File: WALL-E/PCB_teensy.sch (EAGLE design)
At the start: 44 parts

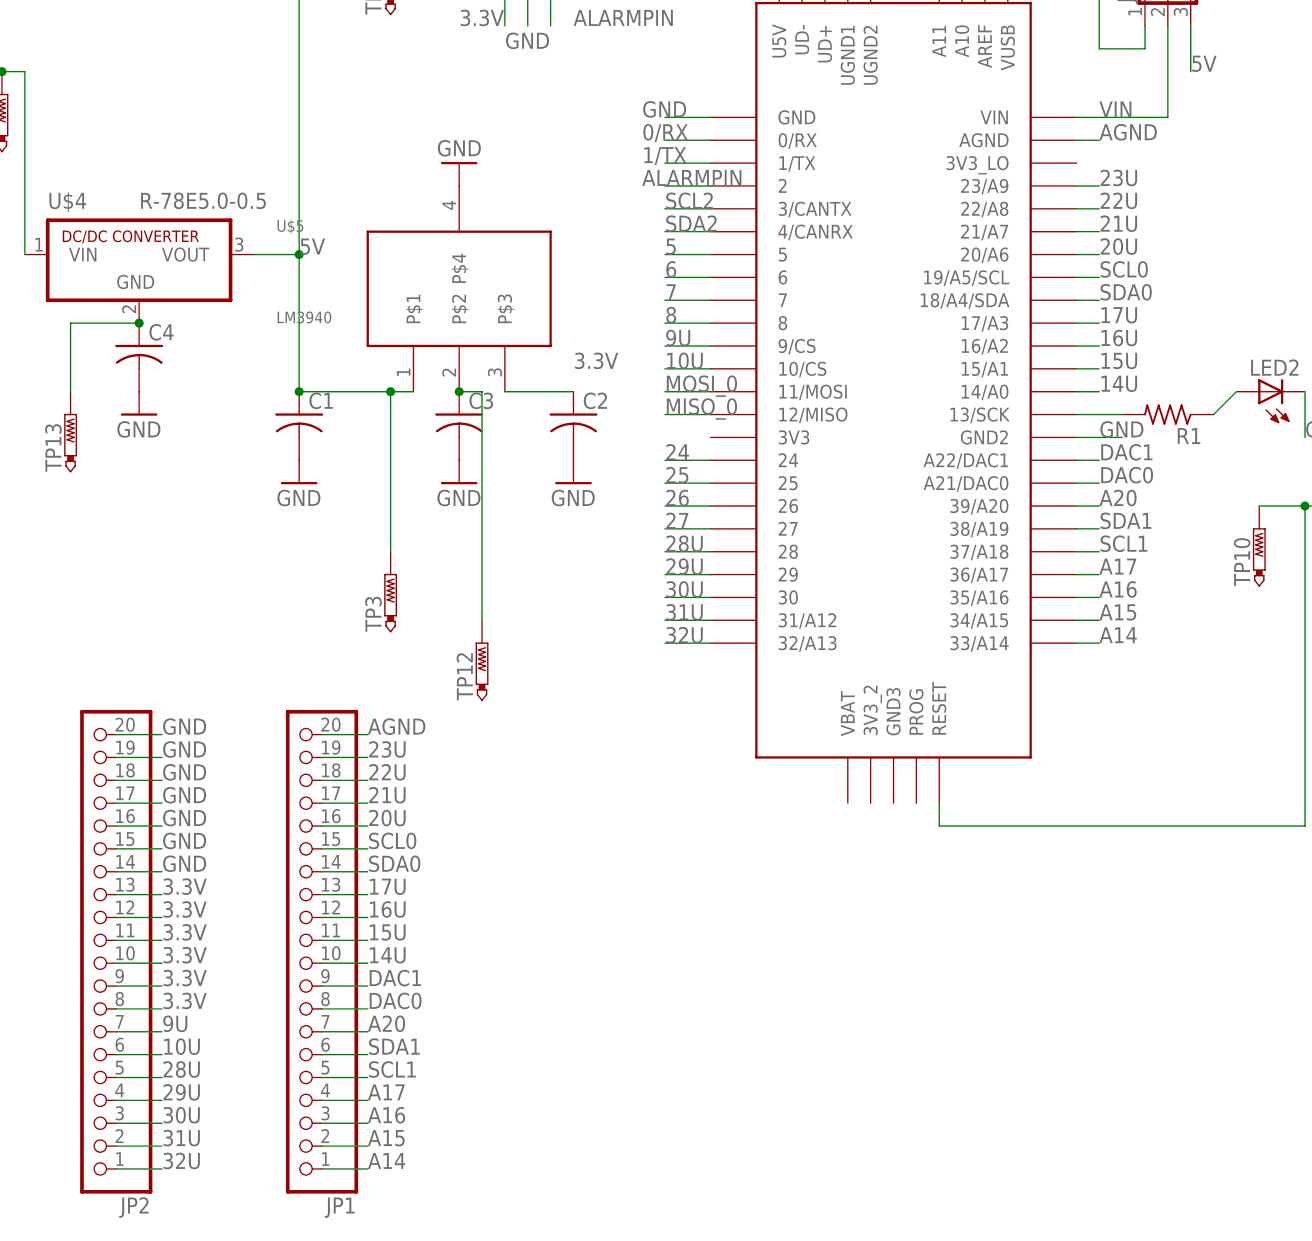
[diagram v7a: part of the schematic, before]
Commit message: Finished wiring the layers besides the tactile switch.
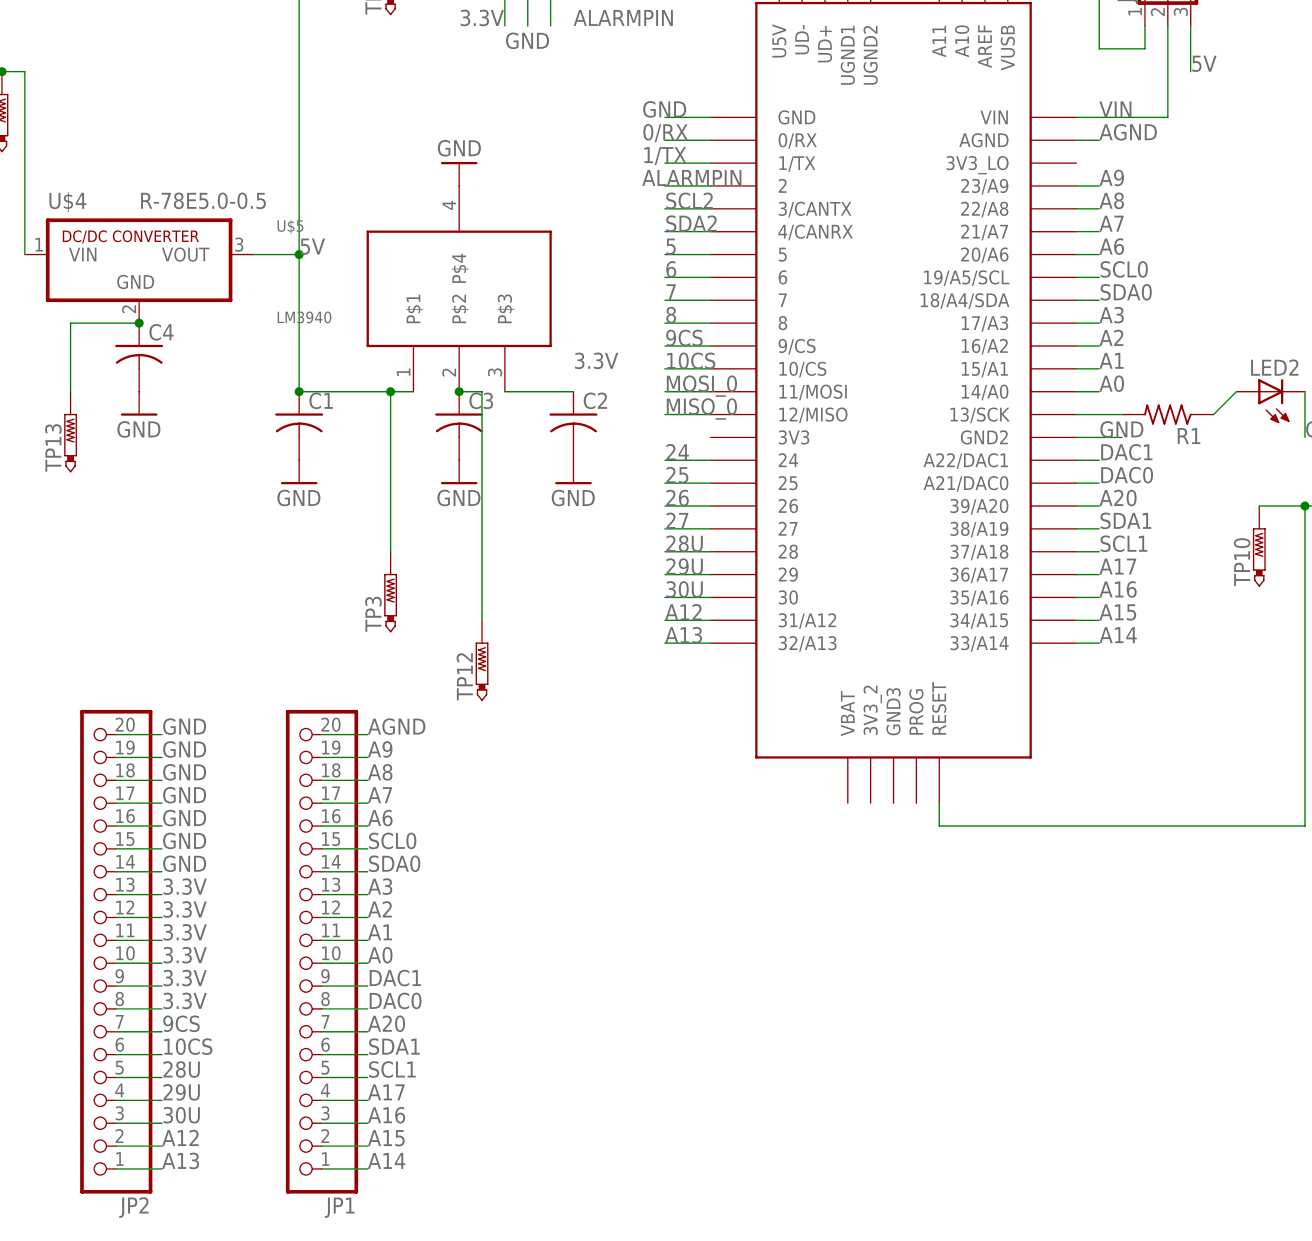
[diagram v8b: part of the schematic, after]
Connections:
- net 10U renamed 10CS
- net 14U renamed A0
- net 15U renamed A1
- net 16U renamed A2
- net 17U renamed A3
- net 20U renamed A6
- net 21U renamed A7
- net 22U renamed A8
- net 23U renamed A9
- net 31U renamed A12
- net 32U renamed A13
- net 9U renamed 9CS
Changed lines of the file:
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@@
 <?xml version="1.0" encoding="utf-8"?>
 <!DOCTYPE eagle SYSTEM "eagle.dtd">
-<eagle version="8.6.3">
+<eagle version="8.6.0">
 <drawing>
 <settings>
@@
 </segment>
 </net>
-<net name="31U" class="0">
+<net name="A12" class="0">
 <segment>
 <pinref part="U$1" gate="G$1" pin="31/A12"/>
@@
 </segment>
 </net>
-<net name="32U" class="0">
+<net name="A13" class="0">
 <segment>
 <pinref part="U$1" gate="G$1" pin="32/A13"/>
@@
 </segment>
 </net>
-<net name="14U" class="0">
+<net name="A0" class="0">
 <segment>
 <pinref part="U$1" gate="G$1" pin="14/A0"/>
@@
 </segment>
 </net>
-<net name="15U" class="0">
+<net name="A1" class="0">
 <segment>
 <pinref part="U$1" gate="G$1" pin="15/A1"/>
@@
 </segment>
 </net>
-<net name="16U" class="0">
+<net name="A2" class="0">
 <segment>
 <pinref part="U$1" gate="G$1" pin="16/A2"/>
@@
 </segment>
 </net>
-<net name="17U" class="0">
+<net name="A3" class="0">
 <segment>
 <pinref part="U$1" gate="G$1" pin="17/A3"/>
@@
 </segment>
 </net>
-<net name="20U" class="0">
+<net name="A6" class="0">
 <segment>
 <pinref part="U$1" gate="G$1" pin="20/A6"/>
@@
 </segment>
 </net>
-<net name="21U" class="0">
+<net name="A7" class="0">
 <segment>
 <pinref part="U$1" gate="G$1" pin="21/A7"/>
@@
 </segment>
 </net>
-<net name="22U" class="0">
+<net name="A8" class="0">
 <segment>
 <pinref part="U$1" gate="G$1" pin="22/A8"/>
@@
 </segment>
 </net>
-<net name="23U" class="0">
+<net name="A9" class="0">
 <segment>
 <pinref part="U$1" gate="G$1" pin="23/A9"/>
@@
 </segment>
 </net>
-<net name="9U" class="0">
+<net name="9CS" class="0">
 <segment>
 <pinref part="U$1" gate="G$1" pin="9/CS"/>
@@
 </segment>
 </net>
-<net name="10U" class="0">
+<net name="10CS" class="0">
 <segment>
 <pinref part="U$1" gate="G$1" pin="10/CS"/>
